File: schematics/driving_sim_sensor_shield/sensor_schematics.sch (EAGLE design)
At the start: 22 parts

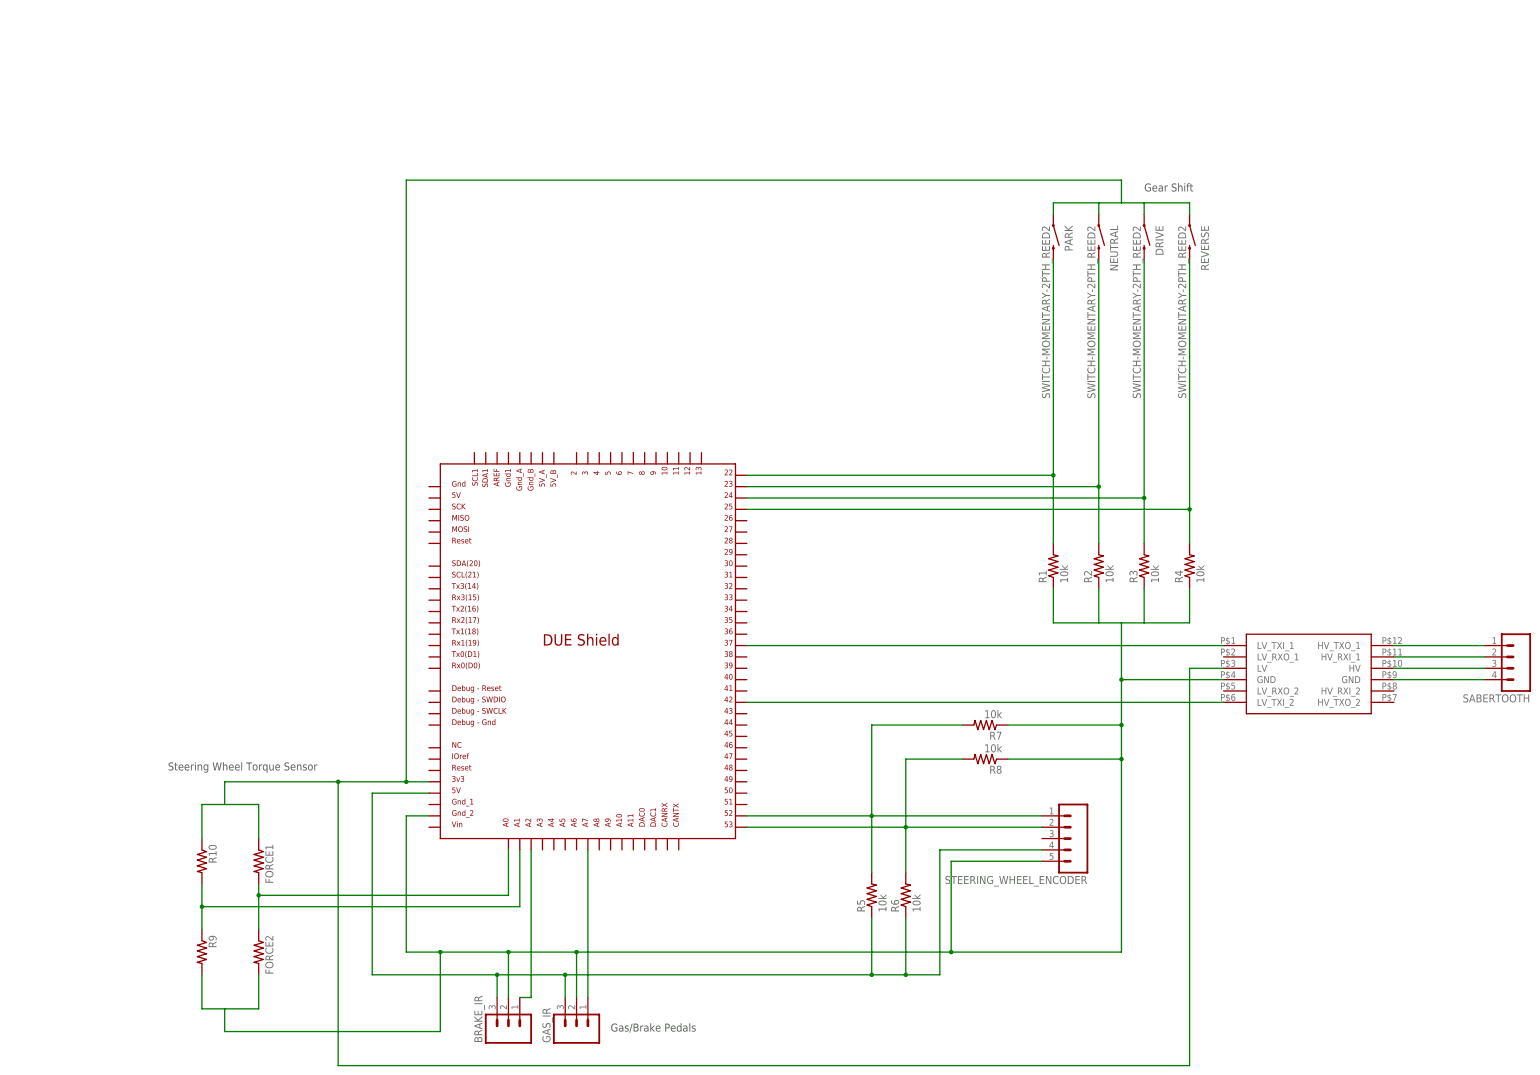
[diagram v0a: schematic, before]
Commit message: Updated schematics for sensors
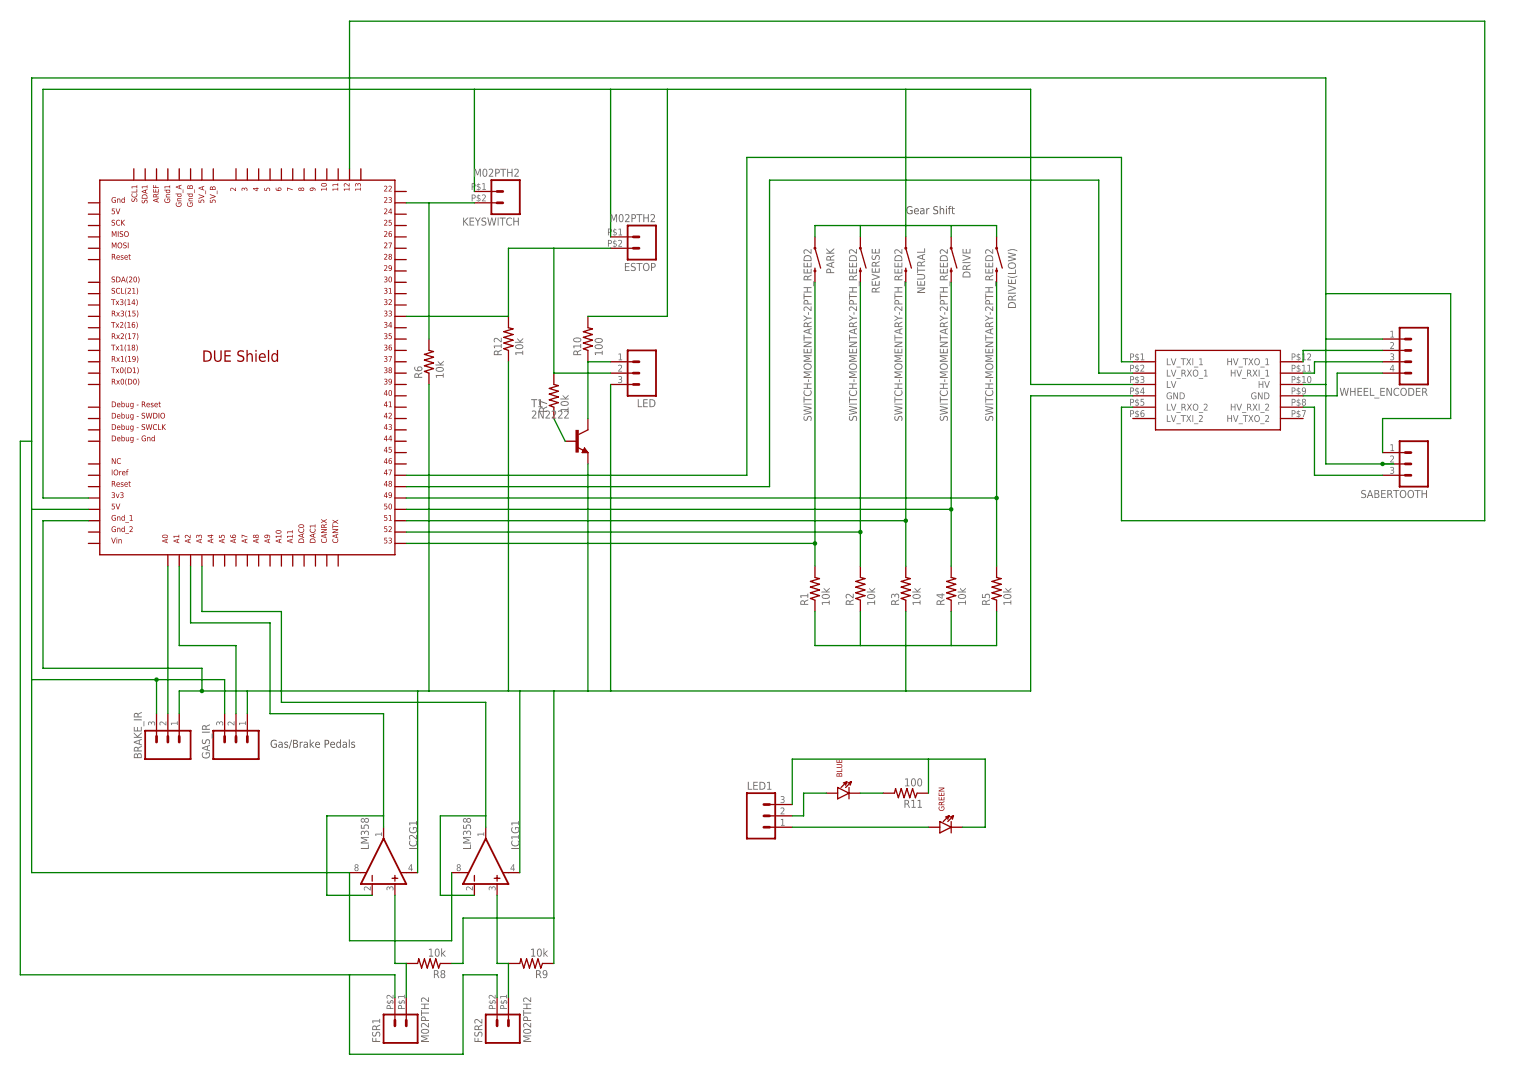
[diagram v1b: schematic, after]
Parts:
- removed FORCE1, FORCE2: (no value), SparkFun-Passives:RESISTOREZ
- removed STEERING_WHEEL_ENCODER: (no value), SparkFun-Connectors:M05PTH
- added BLUE, GREEN: (no value), SparkFun-LED:LTE-302
- added DRIVE(LOW): SWITCH-MOMENTARY-2PTH_REED2, SparkFun-Electromechanical:SWITCH-MOMENTARY-2PTH_REED2
- added ESTOP, FSR1, FSR2, KEYSWITCH: M02PTH2, SparkFun-Connectors:M02PTH2
- added IC1, IC2: LM358, SparkFun-AnalogIC:LM358
- added LED, LED1: (no value), SparkFun-Connectors:M03SCREW
- added R11: 100, SparkFun-Passives:RESISTOREZ
- added R12: 10k, SparkFun-Passives:RESISTOREZ
- added T1: 2N2222, adafruit:2N2222
- added WHEEL_ENCODER: (no value), SparkFun-Connectors:M04PTH
- R10: value (none) -> 100
- R9: value (none) -> 10k
- SABERTOOTH: device SparkFun-Connectors:M04PTH -> SparkFun-Connectors:M03SCREW
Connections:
- new net N$2: DRIVE.1, ESTOP.1, KEYSWITCH.1, NEUTRAL.1, PARK.1, R10.2, REVERSE.1, U$1.3V3, U$2.LV
- new net N$20: IC1G1.-IN, IC1G1.OUT, U$1.A3
- new net N$21: ESTOP.2, LED.2, R12.2, R7.2, U$1.33
- new net N$22: FSR1.1, IC2G1.+IN, R8.2
- new net N$23: BRAKE_IR.1, GAS_IR.1, IC1G1.V-, IC2G1.V-, LED.3, R1.1, R12.1, R2.1, R3.1, R4.1, R6.1, R8.1, R9.1, T1.E, U$1.GND_1, U$2.GND
- new net N$24: FSR2.1, IC1G1.+IN, R9.2
- new net N$25: R7.1, T1.B
- new net N$26: BLUE.A, LED1.2
- new net N$27: LED.1, R10.1, T1.C
- new net N$28: GREEN.A, LED1.1
- new net N$29: GREEN.C, LED1.3, R11.1
- new net N$30: BLUE.C, R11.2
- net N$1: now also DRIVE(LOW).2, R5.2, U$1.49; no longer DRIVE.1, FORCE1.1, NEUTRAL.1, PARK.1, R10.1, REVERSE.1, U$1.3V3, U$2.LV
- net N$10: now also GAS_IR.2, U$1.A1; no longer R5.2, R7.2, STEERING_WHEEL_ENCODER.1, U$1.52
- net N$11: now also SABERTOOTH.3, U$2.HV_RXI_2; no longer SABERTOOTH.1, U$2.HV_TXO_1
- net N$12: now also BRAKE_IR.3, FSR1.2, FSR2.2, GAS_IR.3, IC1G1.V+, IC2G1.V+, SABERTOOTH.1, U$1.5V, U$2.HV, WHEEL_ENCODER.1; no longer U$2.HV_RXI_1
- net N$13: now also KEYSWITCH.2, R6.2, U$1.23; no longer SABERTOOTH.3, U$2.HV
- net N$14: now also WHEEL_ENCODER.4; no longer SABERTOOTH.4
- net N$15: now also U$2.HV_TXO_1, WHEEL_ENCODER.2; no longer U$1.37, U$2.LV_TXI_1
- net N$16: now also U$2.HV_RXI_1, WHEEL_ENCODER.3; no longer U$1.42, U$2.LV_TXI_2
- net N$17: now also U$1.48, U$2.LV_RXO_1; no longer R10.2, R9.1, U$1.A1
- net N$18: now also U$1.12, U$2.LV_RXO_2; no longer FORCE1.2, FORCE2.1, U$1.A0
- net N$19: now also IC2G1.-IN, IC2G1.OUT, U$1.A2; no longer BRAKE_IR.2, FORCE2.2, GAS_IR.2, R1.1, R2.1, R3.1, R4.1, R7.1, R8.1, R9.2, STEERING_WHEEL_ENCODER.5, U$1.GND_2, U$2.GND
- net N$3: now also DRIVE(LOW).1; no longer BRAKE_IR.1, U$1.A2
- net N$4: now also R5.1; no longer GAS_IR.1, U$1.A7
- net N$5: now also REVERSE.2, U$1.52; no longer NEUTRAL.2, U$1.23
- net N$6: now also NEUTRAL.2, U$1.51; no longer DRIVE.2, U$1.24
- net N$7: now also DRIVE.2, U$1.50; no longer REVERSE.2, U$1.25
- net N$8: now also BRAKE_IR.2, U$1.A0; no longer BRAKE_IR.3, GAS_IR.3, R5.1, R6.1, STEERING_WHEEL_ENCODER.4, U$1.5V
- net N$9: now also U$1.47, U$2.LV_TXI_1; no longer R6.2, R8.2, STEERING_WHEEL_ENCODER.2, U$1.53
- net PARK: now also U$1.53; no longer U$1.22
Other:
- note removed: "Steering Wheel Torque Sensor"
- moved on the sheet: BRAKE_IR, DRIVE, GAS_IR, NEUTRAL, PARK, R1, R10, R2, R3, R4, R5, R6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

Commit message: added the pi connections to the schematic
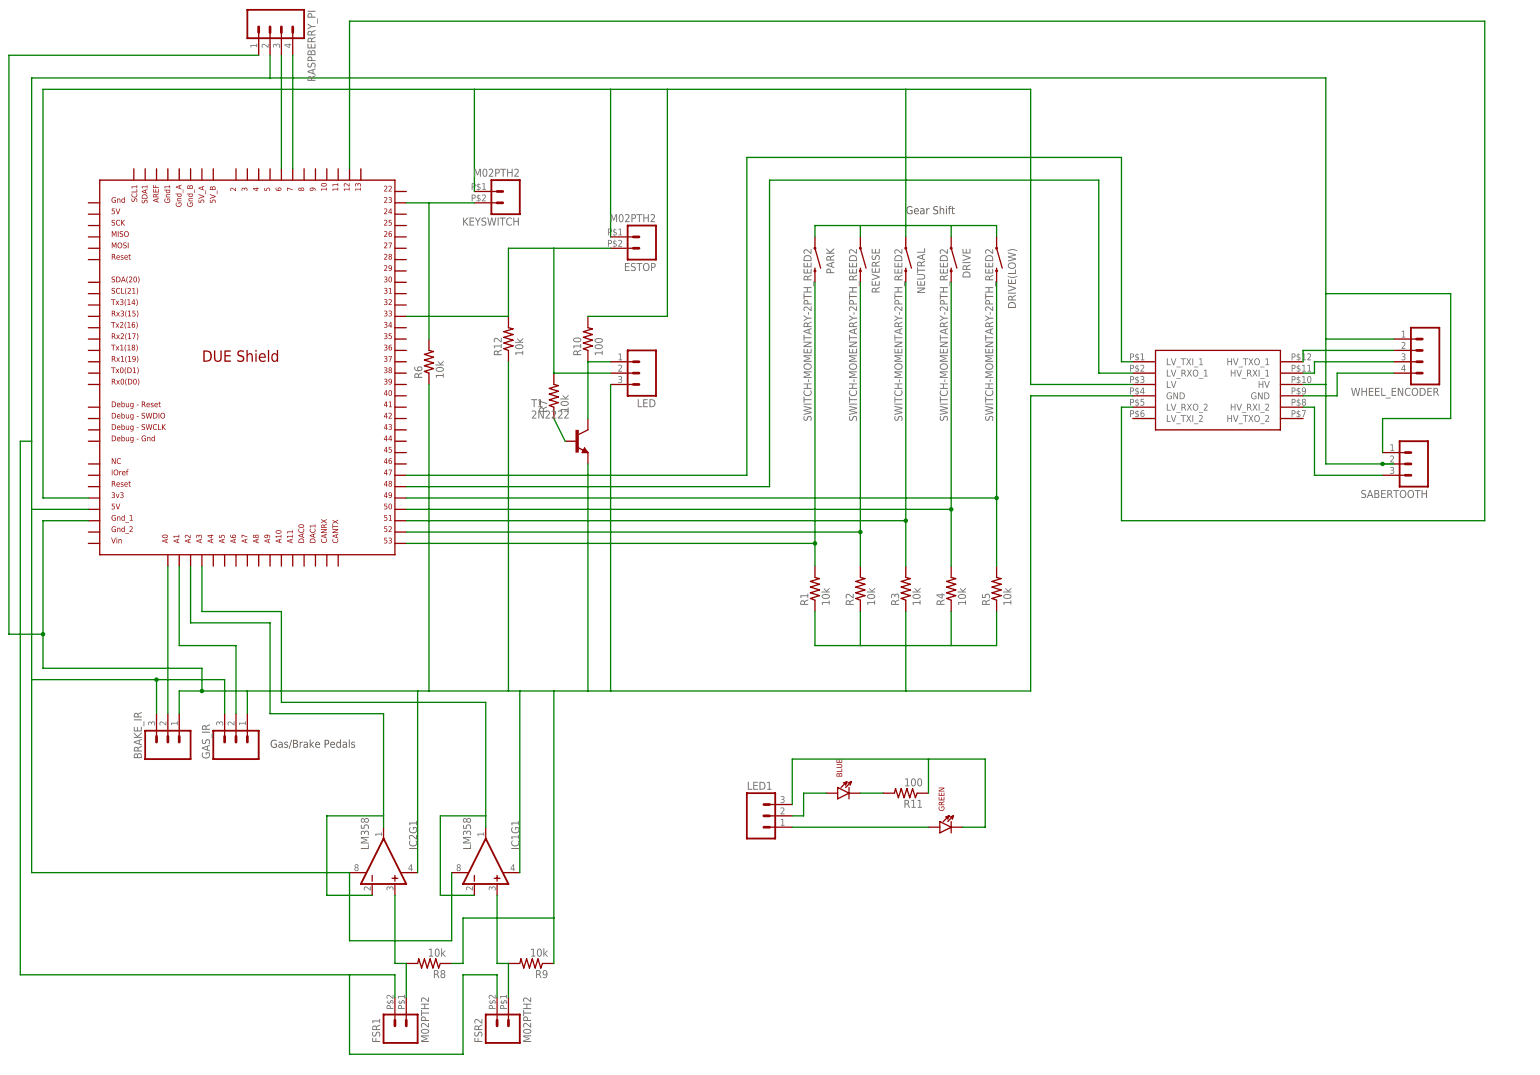
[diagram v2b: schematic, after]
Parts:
- added RASPBERRY_PI: (no value), SparkFun-Connectors:M04PTH
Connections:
- new net N$31: RASPBERRY_PI.3, U$1.6
- new net N$32: RASPBERRY_PI.4, U$1.7
- net N$12: now also RASPBERRY_PI.2
- net N$23: now also RASPBERRY_PI.1
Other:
- moved on the sheet: WHEEL_ENCODER
